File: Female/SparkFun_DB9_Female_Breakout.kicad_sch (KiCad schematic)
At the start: 12 parts, among them J1 DB9-Female, J2 Conn_01x09

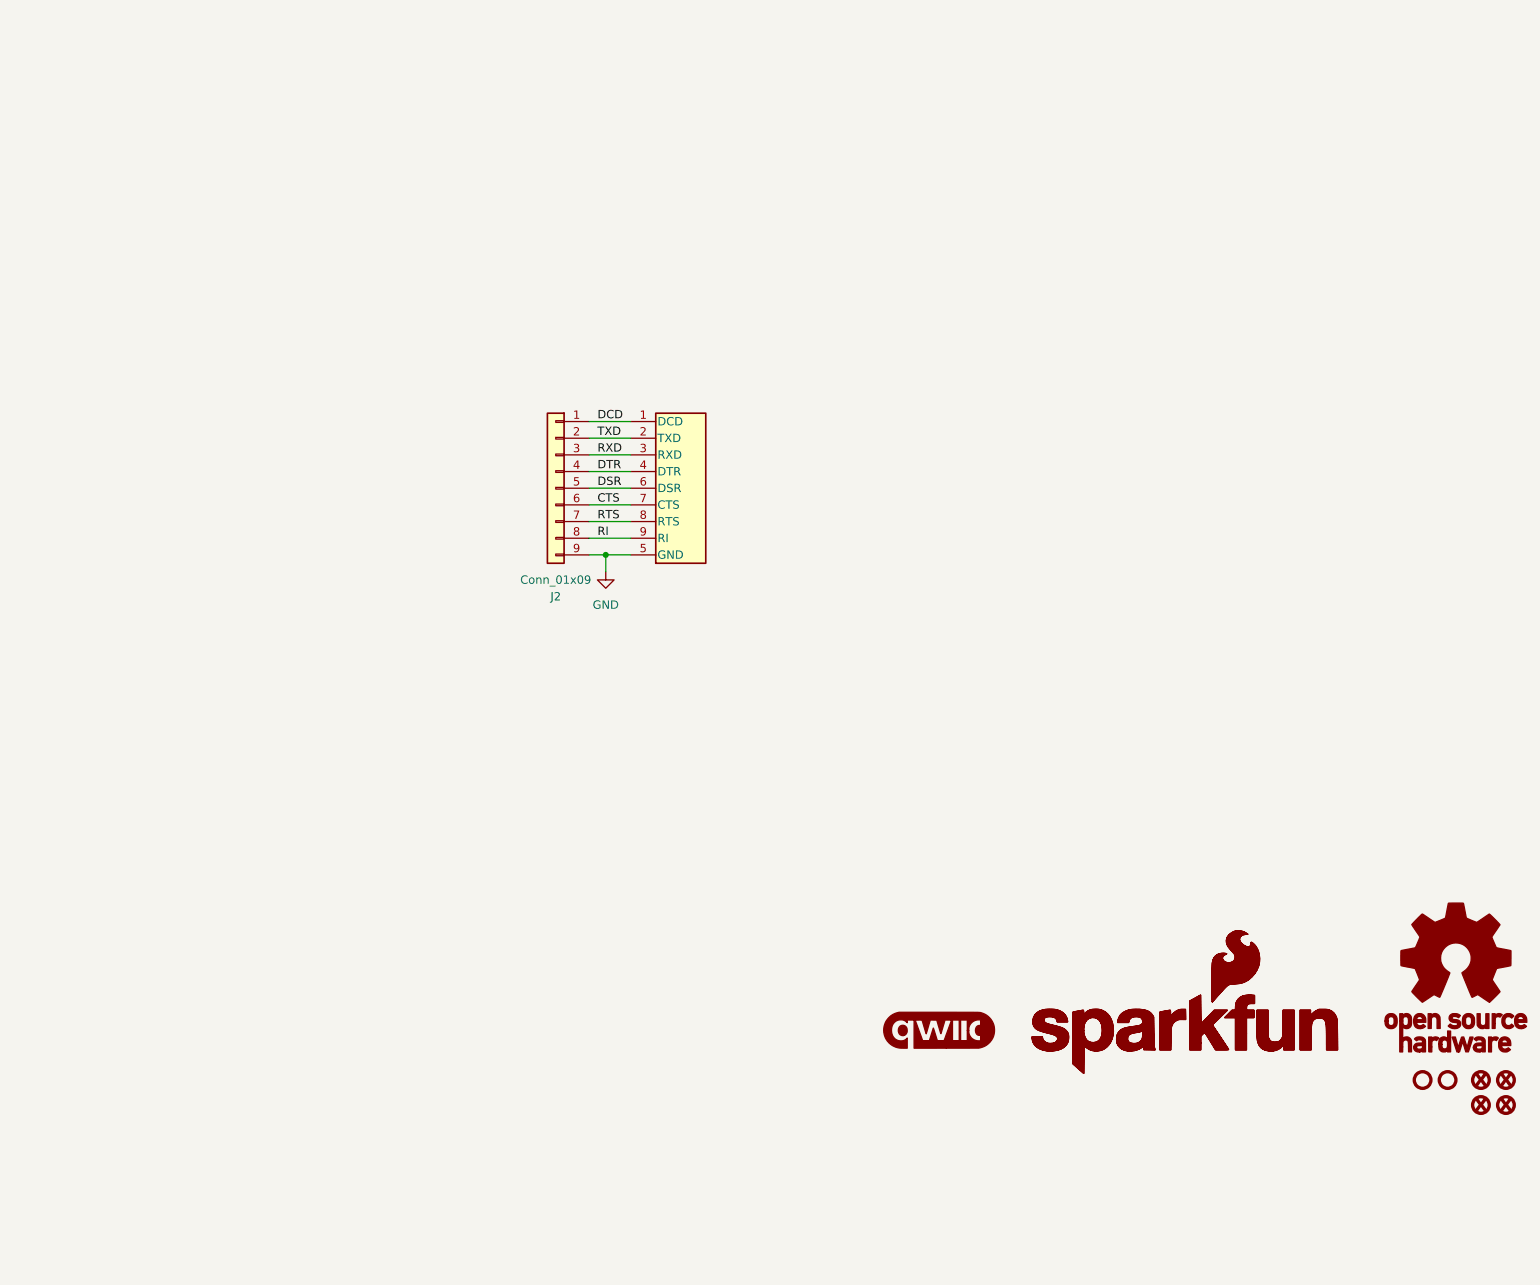
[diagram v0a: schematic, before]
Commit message: Separates male/female design
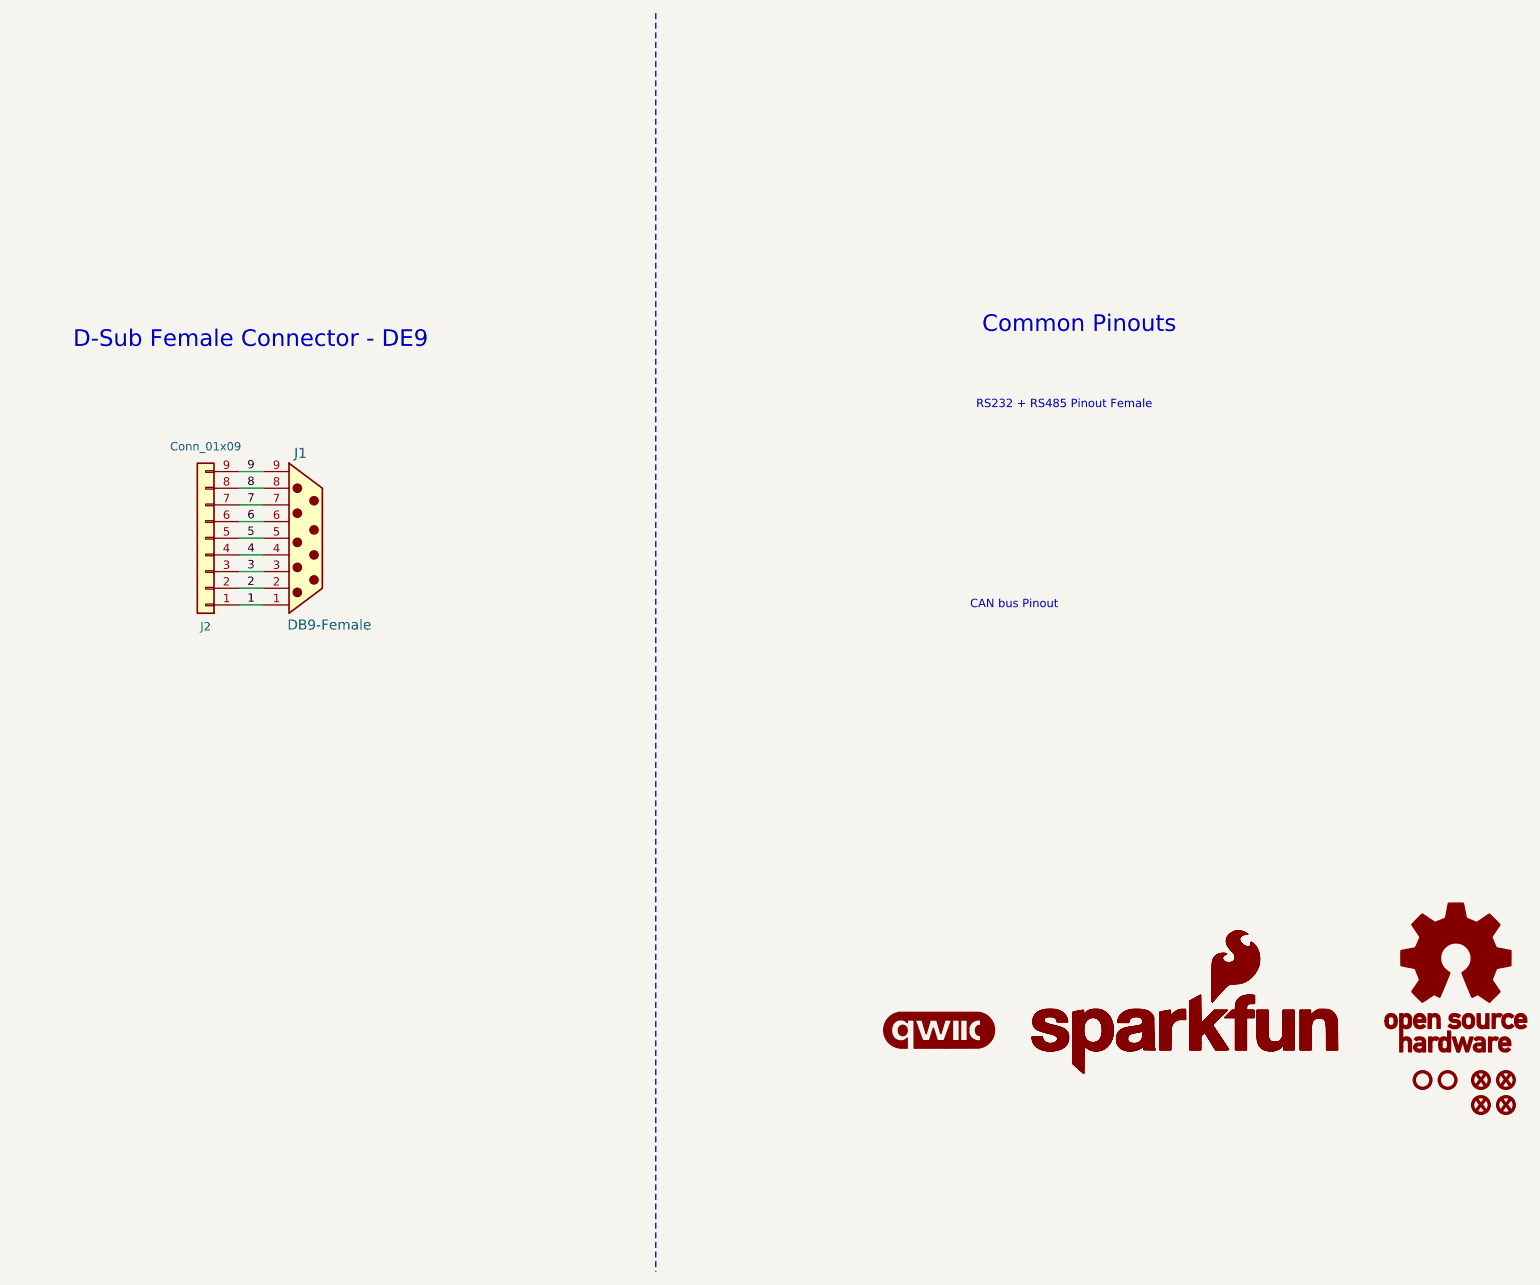
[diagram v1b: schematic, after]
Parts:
- J1: footprint DB9_Footprint:DB9 -> DE9_Footprint:DB9
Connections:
- net CTS renamed 6
- net 6: now also J1.6; no longer J1.7 (CTS)
- net DCD renamed 1
- net DSR renamed 5
- net 5: now also J1.5; no longer J1.6 (DSR)
- net DTR renamed 4
- net GND renamed 9
- net 9: now also J1.9; no longer J1.5 (GND)
- net RI renamed 8
- net 8: now also J1.8; no longer J1.9 (RI)
- net RTS renamed 7
- net 7: now also J1.7; no longer J1.8 (RTS)
- net RXD renamed 3
- net TXD renamed 2
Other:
- note added: "CAN bus Pinout"
- note added: "Common Pinouts"
- note added: "D-Sub Female Connector - DE9"
- note added: "RS232 + RS485 Pinout Female"
- moved on the sheet: J2

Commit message: Adds a male footprint for the DB9 and updates the affected board
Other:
- moved on the sheet: J2
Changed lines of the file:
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@@
+	(wire
+		(pts
+			(xy 69.85 82.55) (xy 73.66 82.55)
+		)
+		(stroke
+			(width 0.2286)
+			(type default)
+		)
+	)
+	(wire
+		(pts
+			(xy 69.85 100.33) (xy 73.66 100.33)
+		)
+		(stroke
+			(width 0)
+			(type default)
+		)
+	)
+	(wire
+		(pts
+			(xy 69.85 87.63) (xy 73.66 87.63)
+		)
+		(stroke
+			(width 0)
+			(type default)
+		)
+	)
+	(polyline
+		(pts
+			(xy 133.35 12.7) (xy 133.35 204.47)
+		)
+		(stroke
+			(width 0)
+			(type dash)
+		)
+	)
+	(wire
+		(pts
+			(xy 69.85 97.79) (xy 73.66 97.79)
+		)
+		(stroke
+			(width 0)
+			(type default)
+		)
+	)
+	(wire
+		(pts
+			(xy 69.85 95.25) (xy 73.66 95.25)
+		)
+		(stroke
+			(width 0)
+			(type default)
+		)
+	)
+	(wire
+		(pts
+			(xy 69.85 90.17) (xy 73.66 90.17)
+		)
+		(stroke
+			(width 0)
+			(type default)
+		)
+	)
 	(wire
 		(pts
@@
 		)
 		(stroke
-			(width 0.2286)
+			(width 0)
 			(type default)
 		)
@@
 		(pts
 			(xy 69.85 85.09) (xy 73.66 85.09)
-		)
-		(stroke
-			(width 0)
-			(type default)
-		)
-	)
-	(wire
-		(pts
-			(xy 69.85 97.79) (xy 73.66 97.79)
-		)
-		(stroke
-			(width 0)
-			(type default)
-		)
-	)
-	(polyline
-		(pts
-			(xy 133.35 12.7) (xy 133.35 204.47)
-		)
-		(stroke
-			(width 0)
-			(type dash)
-		)
-	)
-	(wire
-		(pts
-			(xy 69.85 87.63) (xy 73.66 87.63)
-		)
-		(stroke
-			(width 0)
-			(type default)
-		)
-	)
-	(wire
-		(pts
-			(xy 69.85 90.17) (xy 73.66 90.17)
-		)
-		(stroke
-			(width 0)
-			(type default)
-		)
-	)
-	(wire
-		(pts
-			(xy 69.85 95.25) (xy 73.66 95.25)
-		)
-		(stroke
-			(width 0)
-			(type default)
-		)
-	)
-	(wire
-		(pts
-			(xy 69.85 82.55) (xy 73.66 82.55)
-		)
-		(stroke
-			(width 0)
-			(type default)
-		)
-	)
-	(wire
-		(pts
-			(xy 69.85 100.33) (xy 73.66 100.33)
 		)
 		(stroke
@@
 	)
 	(label "4"
-		(at 71.12 95.25 0)
+		(at 71.12 90.17 0)
 		(effects
 			(font
@@
 	)
 	(label "3"
-		(at 71.12 97.79 0)
+		(at 71.12 87.63 0)
 		(effects
 			(font
@@
 	)
 	(label "9"
-		(at 71.12 82.55 0)
+		(at 71.12 102.87 0)
 		(effects
 			(font
@@
 	)
 	(label "6"
-		(at 71.12 90.17 0)
+		(at 71.12 95.25 0)
 		(effects
 			(font
@@
 	)
 	(label "7"
-		(at 71.12 87.63 0)
+		(at 71.12 97.79 0)
 		(effects
 			(font
@@
 	)
 	(label "1"
-		(at 71.12 102.87 0)
+		(at 71.12 82.55 0)
 		(effects
 			(font
@@
 	)
 	(label "2"
-		(at 71.12 100.33 0)
+		(at 71.12 85.09 0)
 		(effects
 			(font
@@
 	)
 	(label "8"
-		(at 71.12 85.09 0)
+		(at 71.12 100.33 0)
 		(effects
 			(font
@@
 	(symbol
 		(lib_id "SparkFun-Connector:Conn_01x09")
-		(at 64.77 92.71 180)
+		(at 64.77 92.71 0)
+		(mirror y)
 		(unit 1)
 		(exclude_from_sim no)
@@
 		(dnp no)
 		(property "Reference" "J2"
-			(at 64.77 106.172 0)
+			(at 64.77 79.248 0)
 			(effects
 				(font
@@
 		)
 		(property "Value" "Conn_01x09"
-			(at 64.77 78.74 0)
+			(at 64.77 106.68 0)
 			(effects
 				(font
@@
 		)
 		(property "Footprint" "SparkFun-Connector:1x09"
-			(at 64.77 77.47 0)
+			(at 64.77 107.95 0)
 			(effects
 				(font
@@
 		)
 		(property "Datasheet" "~"
-			(at 64.77 74.93 0)
+			(at 64.77 110.49 0)
 			(effects
 				(font
@@
 		)
 		(property "Description" "Basic 0.1\" PTH"
-			(at 64.77 72.39 0)
+			(at 64.77 113.03 0)
 			(effects
 				(font
@@
 		(lib_id "DB9-Female:DB9 Female")
 		(at 80.01 92.71 0)
-		(mirror x)
 		(unit 1)
 		(exclude_from_sim no)
@@
 		(dnp no)
 		(property "Reference" "J1"
-			(at 78.232 79.756 0)
+			(at 78.232 105.664 0)
 			(effects
 				(font
@@
 		)
 		(property "Value" "DB9-Female"
-			(at 77.216 105.918 0)
+			(at 77.216 79.502 0)
 			(effects
 				(font
@@
 		)
 		(property "Footprint" "DE9_Footprint:DB9"
-			(at 80.01 76.454 0)
+			(at 80.01 108.966 0)
 			(effects
 				(font
@@
 		)
 		(property "Datasheet" "https://www.lcsc.com/datasheet/lcsc_datasheet_2411220417_XUNPU-D-SUB-DR-9PCM-CB_C19077337.pdf"
-			(at 80.01 73.914 0)
-			(effects
-				(font
+			(at 80.01 111.506 0)
+			(effects
+				(font

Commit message: Adds gitignore, Fixes Female DB9 Connector, Adds more silk, Adds GND pins
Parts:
- removed FID1, FID2, FID3, FID4: Fiducial_0.5mm, SparkFun-Aesthetic:Fiducial_0.5mm_Mask1mm, symbol SparkFun-Aesthetic:Fiducial_0.5mm
- removed G4: qwiic_Logo, symbol SparkFun-Aesthetic:qwiic_Logo
- added J3, J4: Conn_01x01, SparkFun-Connector:1x01, symbol SparkFun-Connector:Conn_01x01
- J1: footprint DE9_Footprint:DB9 -> DE9_Footprint:DB9_Female
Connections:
- new net GND: J3.1 (Pin_1), J4.1 (Pin_1)
